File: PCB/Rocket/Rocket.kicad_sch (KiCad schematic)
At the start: 47 parts, among them J1 Conn_01x08_Pin, J2 Conn_01x04_Pin, J3 Conn_01x07_Pin, J4 Micro_SD_Card, J5 Conn_ARM_JTAG_SWD_10, J6 Conn_01x04_Pin, J7 1987724, SW1 CK_KMS2xxG, SW2 CK_KMS2xxG, U1 STM32L476RGTx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

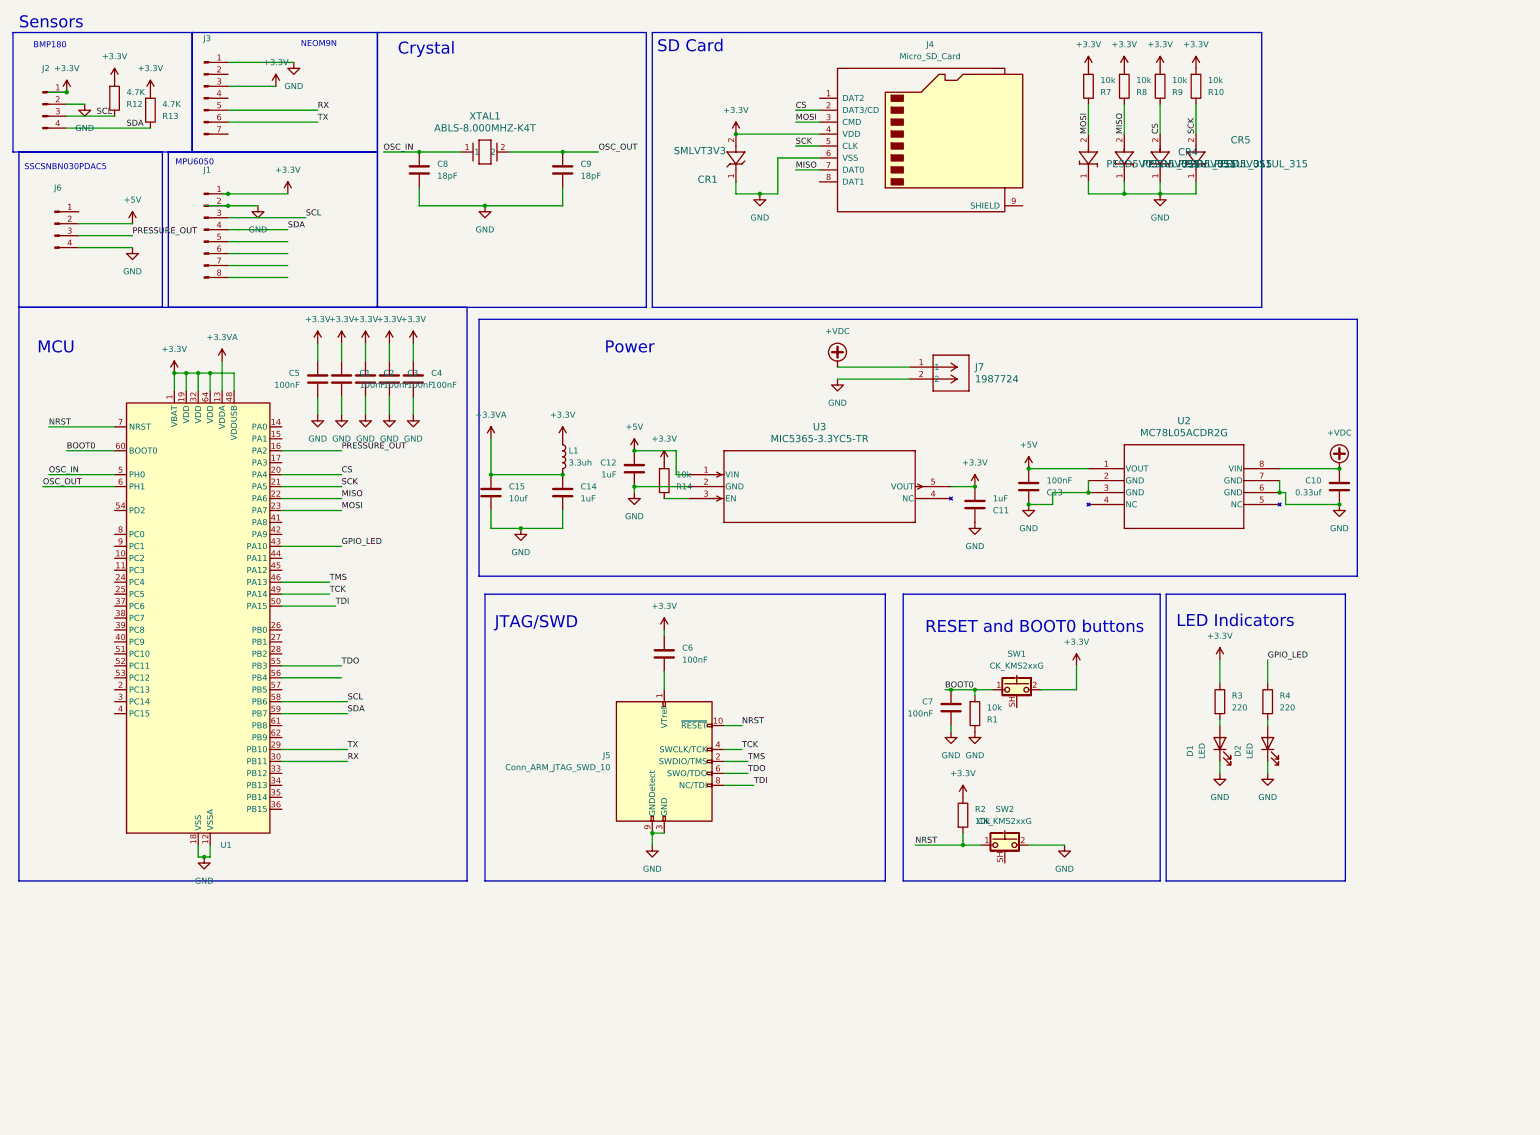
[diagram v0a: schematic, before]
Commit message: Fixed TVS diode and C6 connection.
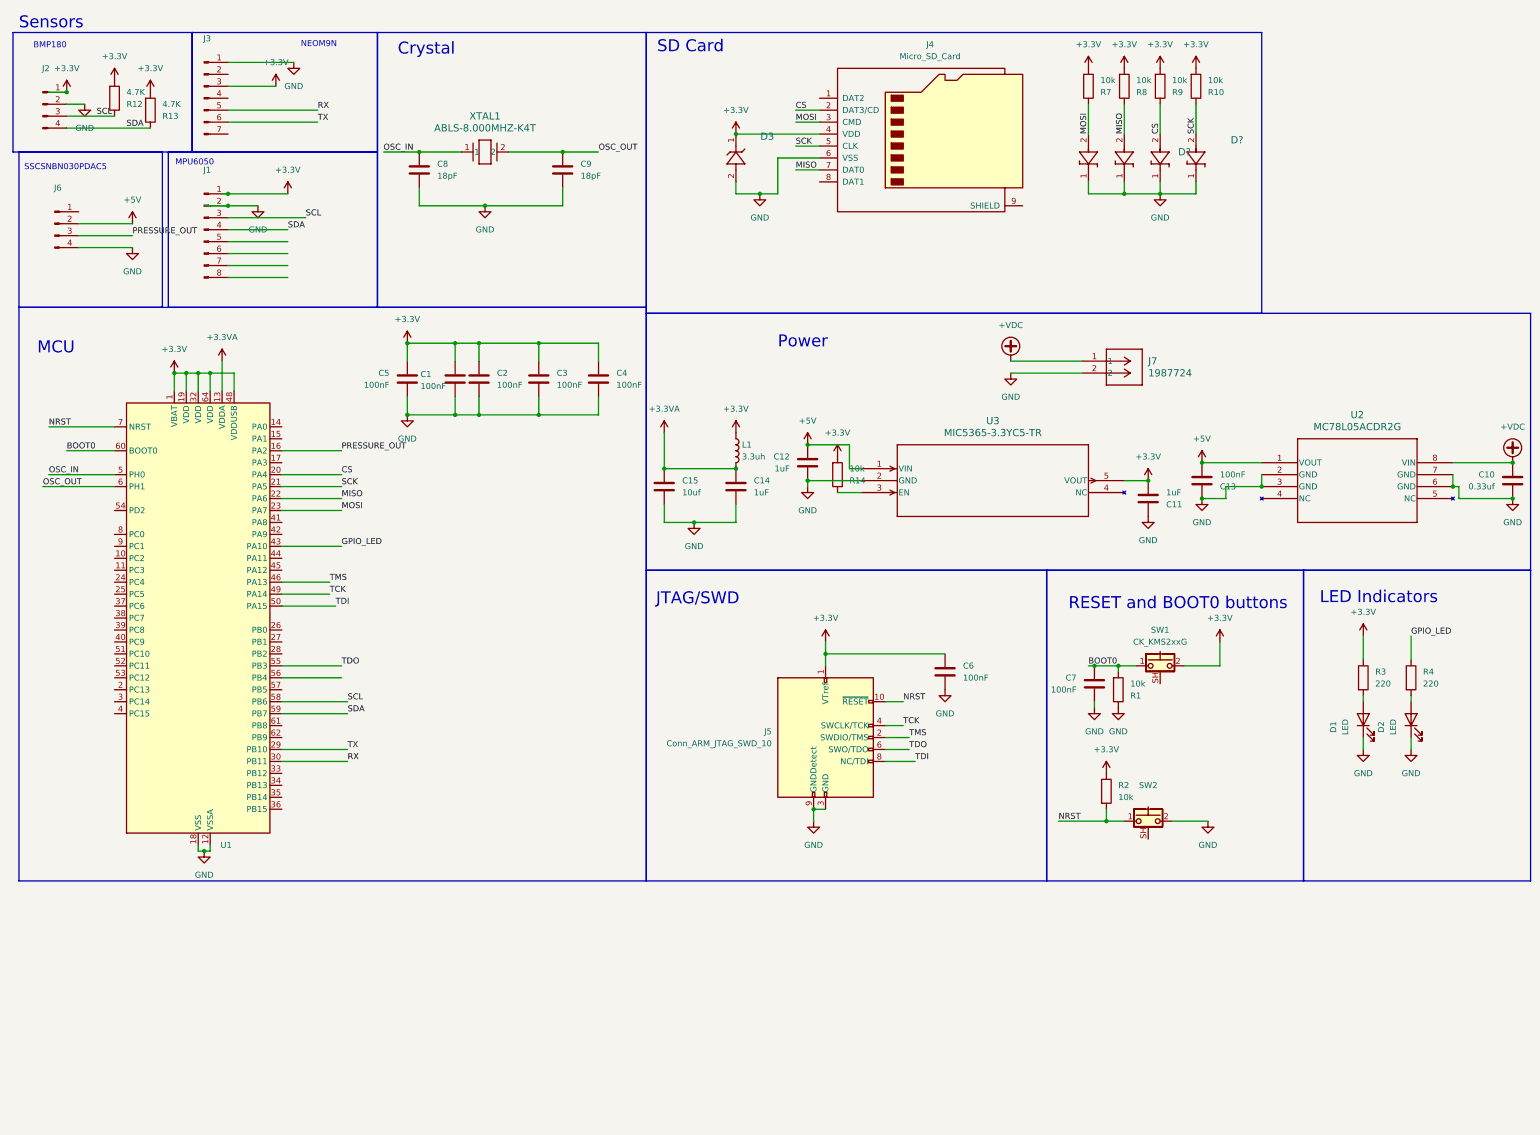
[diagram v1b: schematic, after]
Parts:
- removed CR1: SMLVT3V3, SMLVT3V3:SMB_STM, symbol 2025-01-22_04-11-48:SMLVT3V3
- added D3: SMLVT3V3, SMLVT3V3:SMB_STM, symbol 2025-01-22_04-11-48:SMLVT3V3
- J6: footprint Connector_PinSocket_2.54mm:PinSocket_1x04_P2.54mm_Horizontal -> Connector_PinSocket_2.54mm:PinSocket_1x04_P2.54mm_Vertical
- renumbered CR3 to D?, CR5 to D?, CR4 to D?, CR2 to D?
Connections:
- net +3.3V: now also J5.1 (VTref), D3.1
- net GND: now also C6.2, D3.2
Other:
- moved on the sheet: C1, C10, C11, C12, C13, C14, C15, C2, C3, C4, C5, C7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

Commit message: Updated footprints for regulators and silkscreen.
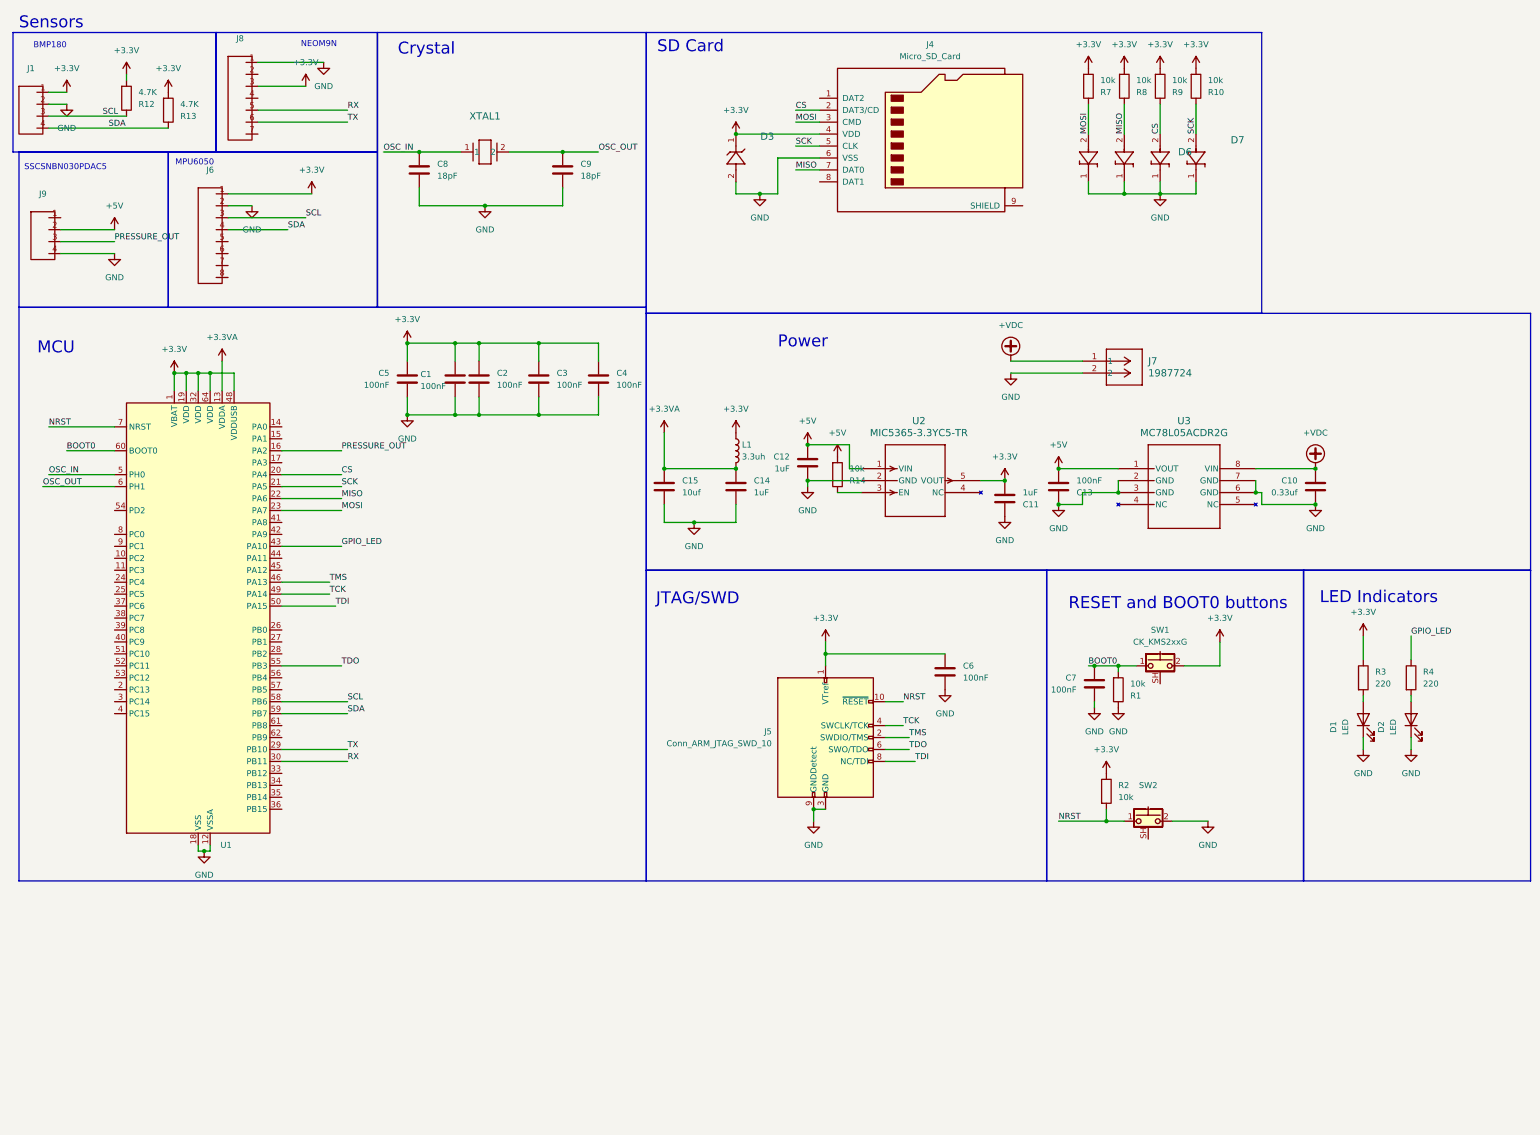
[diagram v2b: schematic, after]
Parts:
- removed J1: Conn_01x08_Pin, Connector_PinSocket_2.54mm:PinSocket_1x08_P2.54mm_Vertical, symbol Connector:Conn_01x08_Pin
- removed J2, J6: Conn_01x04_Pin, Connector_PinSocket_2.54mm:PinSocket_1x04_P2.54mm_Vertical, symbol Connector:Conn_01x04_Pin
- removed J3: Conn_01x07_Pin, Connector_PinSocket_2.54mm:PinSocket_1x07_P2.54mm_Vertical, symbol Connector:Conn_01x07_Pin
- removed U2: MC78L05ACDR2G, MC78L05ACDR2G:SOIC8_ONS, symbol MC78L05ACDR2G:MC78L05ACDR2G
- removed U3: MIC5365-3.3YC5-TR, MIC5365-3.3YC5-TR:SC-70_C5_MCH, symbol MIC5365-3.3YC5-TR:MIC5365-3.3YC5-TR
- added J1, J9: ~, Connector_PinSocket_2.54mm:PinSocket_1x04_P2.54mm_Vertical, symbol Conn_1x04:Conn_1x04
- added J6: ~, Connector_PinSocket_2.54mm:PinSocket_1x08_P2.54mm_Vertical, symbol Conn_1x04:Conn_1x08
- added J8: ~, Connector_PinSocket_2.54mm:PinSocket_1x07_P2.54mm_Vertical, symbol Conn_1x04:Conn_1x07
- added U2: MIC5365-3.3YC5-TR, MC78L05ACDR2G:SOIC8_ONS, symbol MIC5365-3.3YC5-TR:MIC5365-3.3YC5-TR
- added U3: MC78L05ACDR2G, MC78L05ACDR2G:SOIC8_ONS, symbol MC78L05ACDR2G:MC78L05ACDR2G
- gave numbers to parts that had none: 4
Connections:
- net +3.3V: now also J1.1, J6.1, J8.3, U2.5 (VOUT); no longer R14.2
- net +5V: now also R14.2, J9.2, U2.1 (VIN), U3.1 (VOUT)
- net +VDC: now also U3.8 (VIN)
- net GND: now also J1.2, J6.2, J8.1, J9.4, U2.2 (GND), U3.2 (GND), U3.3 (GND), U3.6 (GND), U3.7 (GND)
- net PRESSURE_OUT: now also J9.3
- net RX: now also J8.5
- net SCL: now also J1.3, J6.3
- net SDA: now also J1.4, J6.4
- net TX: now also J8.6
- net at R14.1: now also U2.3 (EN)
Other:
- moved on the sheet: C10, C11, C13, R12, R13

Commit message: Updating to use arduino instead of STM32
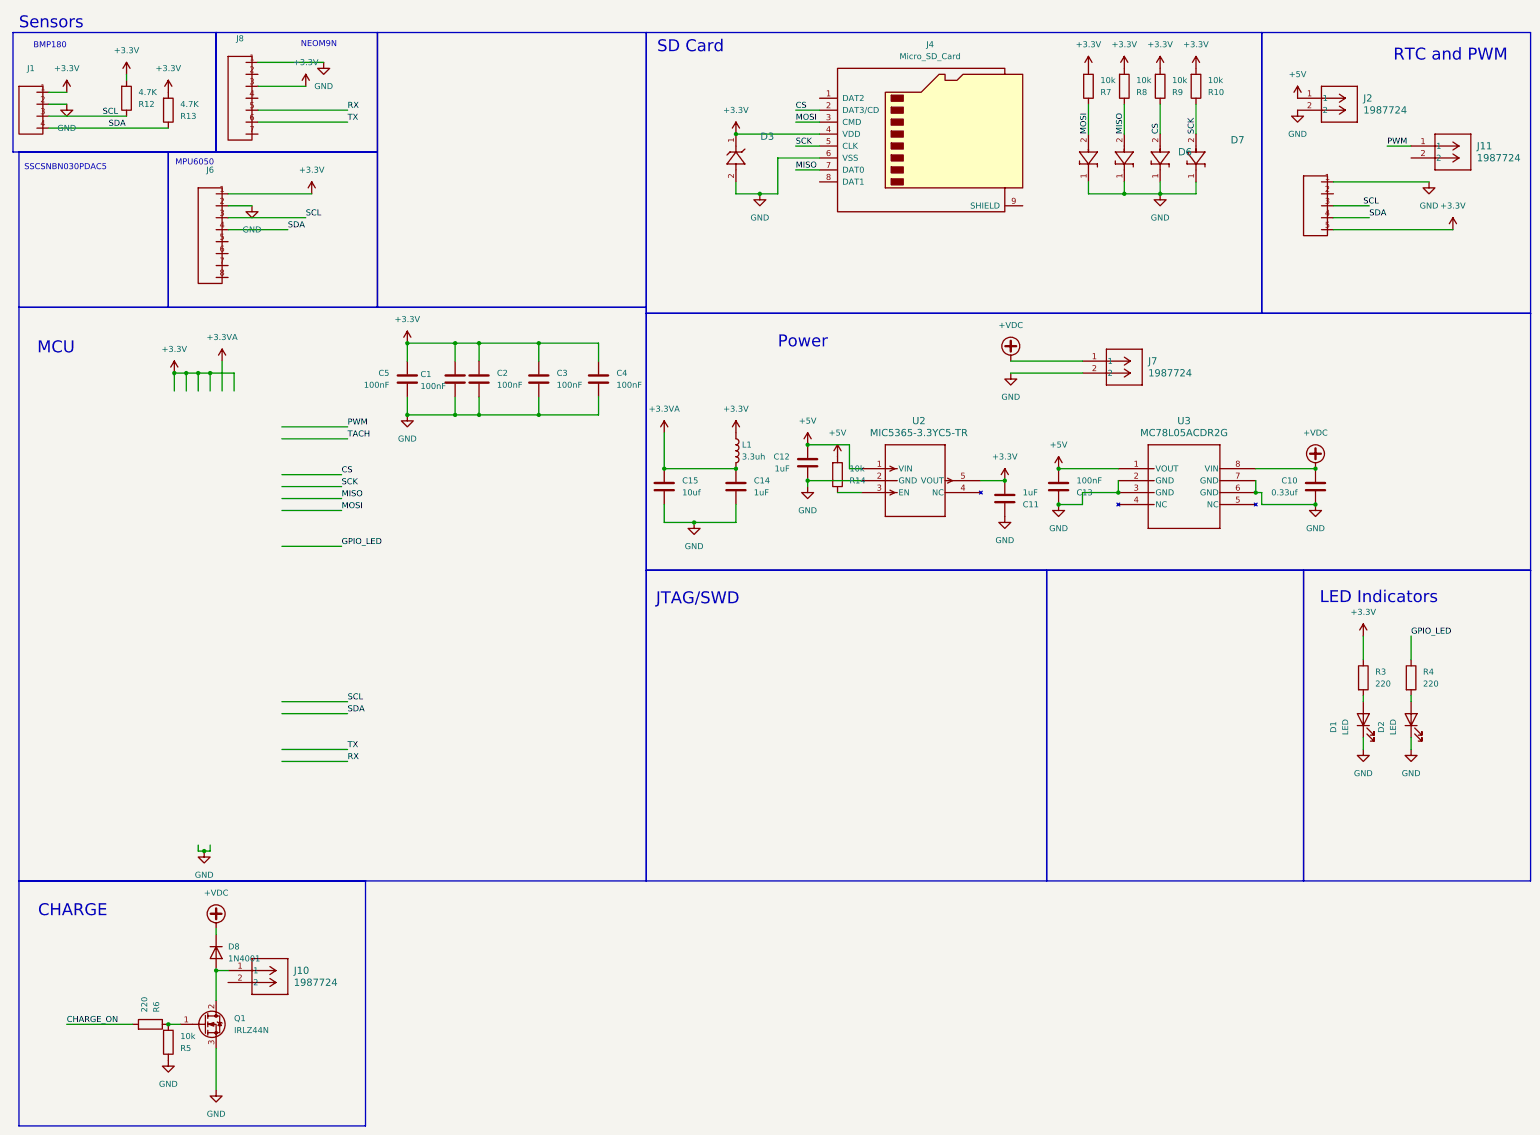
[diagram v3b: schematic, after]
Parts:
- removed C6, C7: 100nF, Capacitor_SMD:C_0201_0603Metric, symbol Device:C
- removed C8, C9: 18pF, Capacitor_SMD:C_0201_0603Metric, symbol Device:C
- removed J5: Conn_ARM_JTAG_SWD_10, 3221_10_0300_00:CONN10_3221-10-0300-00_CNC, symbol Connector:Conn_ARM_JTAG_SWD_10
- removed J9: ~, Connector_PinSocket_2.54mm:PinSocket_1x04_P2.54mm_Vertical, symbol Conn_1x04:Conn_1x04
- removed R1, R2: 10k, Resistor_SMD:R_0201_0603Metric_Pad0.64x0.40mm_HandSolder, symbol Device:R
- removed SW1, SW2: CK_KMS2xxG, Button_Switch_SMD:SW_SPST_CK_KMS2xxGP, symbol Switch:CK_KMS2xxG
- removed U1: STM32L476RGTx, Package_QFP:LQFP-64_10x10mm_P0.5mm, symbol MCU_ST_STM32L4:STM32L476RGTx
- removed XTAL1: ABLS-8.000MHZ-K4T, ABLS-8.000MHZ-K4T:CRYSTAL_ABLS-8.000MHZ-K4T_ABR, symbol ABLS-8.000MHZ-K4T:ABLS-8.000MHZ-K4T
- added D8: 1N4001, Diode_THT:D_DO-41_SOD81_P10.16mm_Horizontal, symbol Diode:1N4001
- added J10, J11, J2: 1987724, 1987724:CONN_1987724_PXC, symbol 1987724:1987724
- added J3: ~, Connector_Molex:Molex_KK-254_AE-6410-05A_1x05_P2.54mm_Vertical, symbol Conn_1x04:Conn_1x05
- added Q1: IRLZ44N, Package_TO_SOT_THT:TO-220-3_Vertical, symbol Transistor_FET:IRLZ44N
- added R5: 10k, Resistor_SMD:R_0201_0603Metric_Pad0.64x0.40mm_HandSolder, symbol Device:R
- added R6: 220, Resistor_SMD:R_0201_0603Metric_Pad0.64x0.40mm_HandSolder, symbol Device:R
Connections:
- net +3.3V: now also J3.5
- net +5V: now also J2.1
- net +VDC: now also D8.1 (K)
- net GND: now also J2.2, J3.1, Q1.3 (S), R5.1
- net SCL: now also J3.3
- net SDA: now also J3.4
- new net: Q1.1 (G), R5.2, R6.1
- new net: D8.2 (A), J10.1, Q1.2 (D)
- new net CHARGE_ON: R6.2
- new net PWM: J11.1
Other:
- note added: "CHARGE"
- note added: "RTC and PWM"
- note removed: "Crystal"
- note removed: "RESET and BOOT0 buttons"

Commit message: Updated PCB
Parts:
- removed C1, C2, C3, C4, C5: 100nF, Capacitor_SMD:C_0201_0603Metric, symbol Device:C
- removed D8: 1N4001, Diode_THT:D_DO-41_SOD81_P10.16mm_Horizontal, symbol Diode:1N4001
- removed J10: 1987724, 1987724:CONN_1987724_PXC, symbol 1987724:1987724
- removed Q1: IRLZ44N, Package_TO_SOT_THT:TO-220-3_Vertical, symbol Transistor_FET:IRLZ44N
- removed R5: 10k, Resistor_SMD:R_0201_0603Metric_Pad0.64x0.40mm_HandSolder, symbol Device:R
- removed R6: 220, Resistor_SMD:R_0201_0603Metric_Pad0.64x0.40mm_HandSolder, symbol Device:R
- added U1: ATMEGA328P-PN, 28P3_ATM, symbol Arduino:ATMEGA328P-PN
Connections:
- net +5V: now also U1.7 (VCC)
- net CS: now also U1.16 (PB2)
- net GND: now also U1.8 (GND)
- net MISO: now also U1.18 (PB4)
- net MOSI: now also U1.19 (PB5)
- net PWM: now also U1.23 (PC0)
- net RX: now also U1.13 (PD7)
- net SCK: now also U1.17 (PB3)
- net SCL: now also U1.28 (PC5)
- net SDA: now also U1.27 (PC4)
- net TX: now also U1.14 (PB0)
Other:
- note removed: "CHARGE"
- note removed: "JTAG/SWD"
- note removed: "SSCSNBN030PDAC5"
